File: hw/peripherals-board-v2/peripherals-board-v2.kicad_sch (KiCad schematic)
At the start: 8 parts, among them J1 Screw_Terminal_01x04, J2 Conn_01x04_Socket, U2 M24C01-FMN, U4 AMS1117-5.0

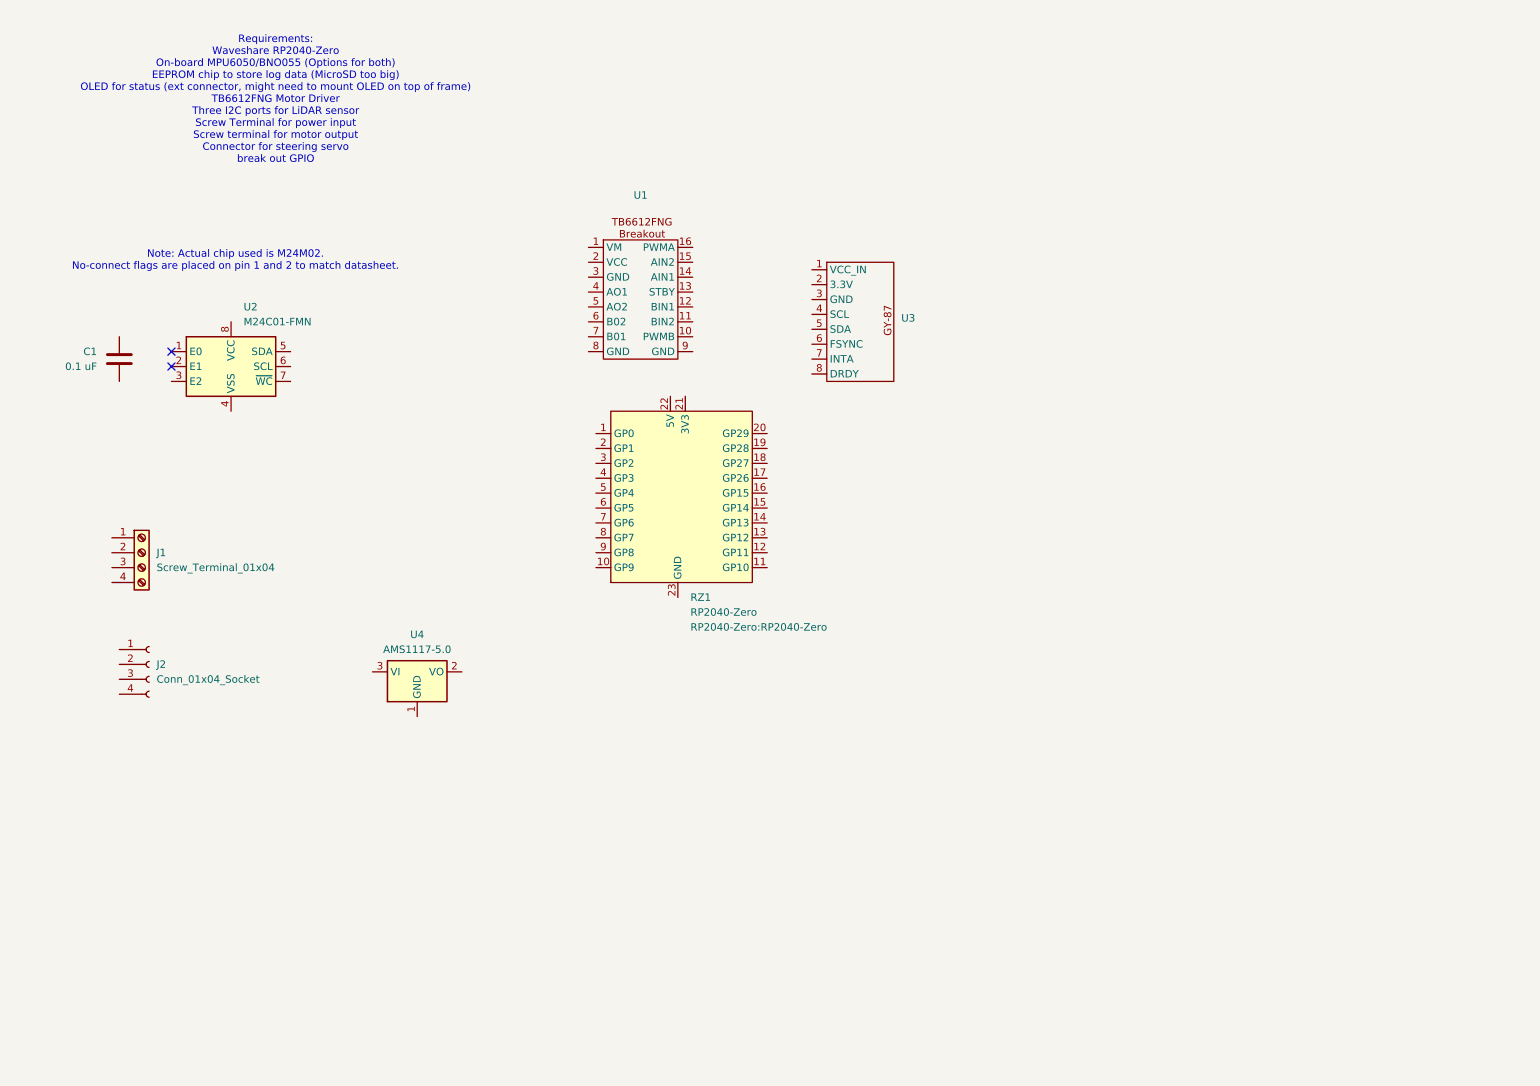
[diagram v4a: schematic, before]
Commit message: Revision 1 of PCB layout, create footprints, generate interactive BOM
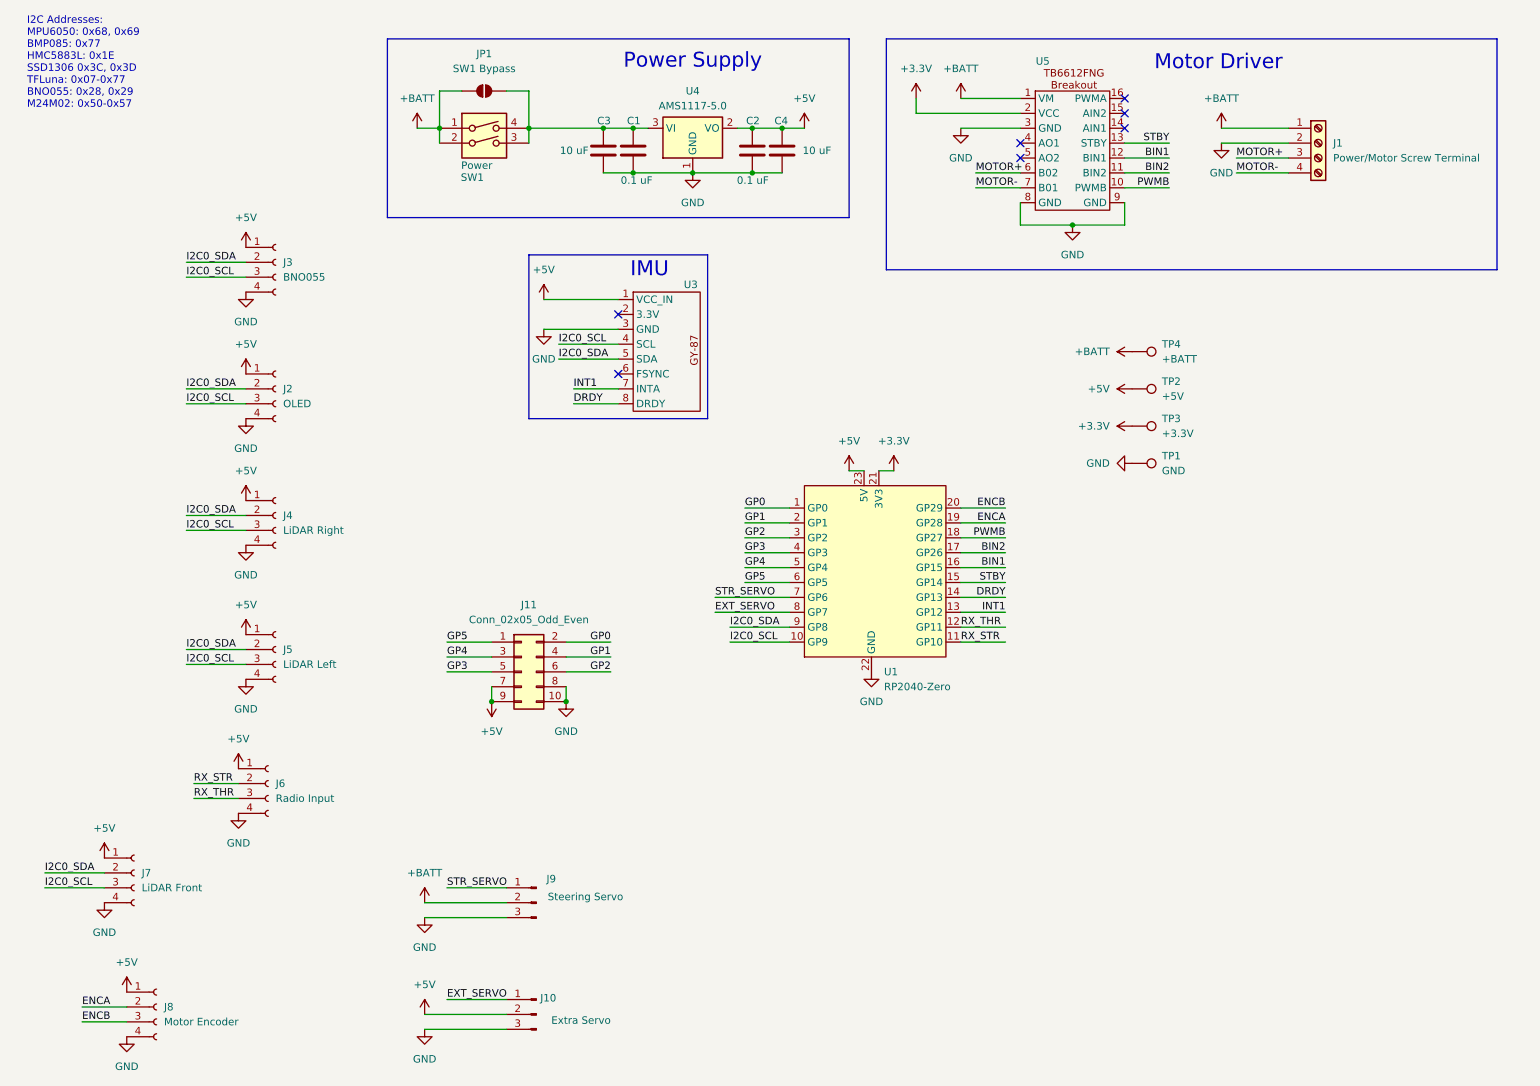
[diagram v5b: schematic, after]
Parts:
- removed U2: M24C01-FMN, Package_SO:SOIC-8_3.9x4.9mm_P1.27mm, symbol Memory_EEPROM:M24C01-FMN
- added C2: 0.1 uF, Capacitor_SMD:C_0805_2012Metric_Pad1.18x1.45mm_HandSolder, symbol Device:C
- added C3, C4: 10 uF, Capacitor_SMD:C_0805_2012Metric_Pad1.18x1.45mm_HandSolder, symbol Device:C
- added J10: Extra Servo, Connector_PinHeader_2.54mm:PinHeader_1x03_P2.54mm_Vertical, symbol Connector:Conn_01x03_Pin
- added J11: Conn_02x05_Odd_Even, Connector_PinSocket_2.54mm:PinSocket_2x05_P2.54mm_Vertical, symbol Connector_Generic:Conn_02x05_Odd_Even
- added J3: BNO055, Connector_JST:JST_EH_S4B-EH_1x04_P2.50mm_Horizontal, symbol Connector:Conn_01x04_Socket
- added J4: LiDAR Right, Connector_JST:JST_EH_S4B-EH_1x04_P2.50mm_Horizontal, symbol Connector:Conn_01x04_Socket
- added J5: LiDAR Left, Connector_JST:JST_EH_S4B-EH_1x04_P2.50mm_Horizontal, symbol Connector:Conn_01x04_Socket
- added J6: Radio Input, Connector_JST:JST_EH_S4B-EH_1x04_P2.50mm_Horizontal, symbol Connector:Conn_01x04_Socket
- added J7: LiDAR Front, Connector_JST:JST_EH_S4B-EH_1x04_P2.50mm_Horizontal, symbol Connector:Conn_01x04_Socket
- added J8: Motor Encoder, Connector_JST:JST_EH_S4B-EH_1x04_P2.50mm_Horizontal, symbol Connector:Conn_01x04_Socket
- added J9: Steering Servo, Connector_PinHeader_2.54mm:PinHeader_1x03_P2.54mm_Vertical, symbol Connector:Conn_01x03_Pin
- added JP1: SW1 Bypass, Jumper:SolderJumper-2_P1.3mm_Open_RoundedPad1.0x1.5mm, symbol Jumper:SolderJumper_2_Open
- added SW1: Power, Package_DIP:DIP-4_W7.62mm, symbol Switch:SW_DIP_x02
- added TP1: GND, TestPoint:TestPoint_Pad_D1.5mm, symbol Connector:TestPoint
- added TP2: +5V, TestPoint:TestPoint_Pad_D1.5mm, symbol Connector:TestPoint
- added TP3: +3.3V, TestPoint:TestPoint_Pad_D1.5mm, symbol Connector:TestPoint
- added TP4: +BATT, TestPoint:TestPoint_Pad_D1.5mm, symbol Connector:TestPoint
- J1: value Screw_Terminal_01x04 -> Power/Motor Screw Terminal
- J2: value Conn_01x04_Socket -> OLED
- U4: footprint Package_TO_SOT_SMD:TO-263-2 -> Package_TO_SOT_SMD:SOT-223-3_TabPin2
- renumbered RZ1 to U1, U1 to U5
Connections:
- net GP0: now reaches U1.1 (GP0)
- net GP0: now also J11.2 (Pin_2)
- net I2C0_SCL: now reaches U1.10 (GP9)
- net I2C0_SCL: now also J2.3 (Pin_3), U3.4 (SCL), J3.3 (Pin_3), J4.3 (Pin_3), J5.3 (Pin_3), J7.3 (Pin_3)
- net RX_STR: now reaches U1.11 (GP10)
- net RX_STR: now also J6.2 (Pin_2)
- net RX_THR: now reaches U1.12 (GP11)
- net RX_THR: now also J6.3 (Pin_3)
- net INT1: now reaches U1.13 (GP12)
- net INT1: now also U3.7 (INTA)
- net DRDY: now reaches U1.14 (GP13)
- net DRDY: now also U3.8 (DRDY)
- net STBY: now reaches U1.15 (GP14)
- net STBY: now also U5.13 (STBY)
- net BIN1: now reaches U1.16 (GP15)
- net BIN1: now also U5.12 (BIN1)
- net BIN2: now reaches U1.17 (GP26)
- net BIN2: now also U5.11 (BIN2)
- net PWMB: now reaches U1.18 (GP27)
- net PWMB: now also U5.10 (PWMB)
- net ENCA: now reaches U1.19 (GP28)
- net ENCA: now also J8.2 (Pin_2)
- net GP1: now reaches U1.2 (GP1)
- net GP1: now also J11.4 (Pin_4)
- net ENCB: now reaches U1.20 (GP29)
- net ENCB: now also J8.3 (Pin_3)
- net +3.3V: now reaches U1.21 (3V3)
- net +3.3V: now also U5.2 (VCC), TP3.1
- net GND: now reaches U1.22 (GND)
- net GND: now also C1.2, J1.2 (Pin_2), J2.4 (Pin_4), U3.3 (GND), U4.1 (GND), U5.3 (GND), U5.8 (GND), U5.9 (GND), C2.2, C3.2, C4.2, J10.3 (Pin_3), J11.10 (Pin_10), J11.8 (Pin_8), J3.4 (Pin_4), J4.4 (Pin_4), J5.4 (Pin_4), J6.4 (Pin_4), J7.4 (Pin_4), J8.4 (Pin_4), J9.3 (Pin_3), TP1.1
- net +5V: now reaches U1.23 (5V)
- net +5V: now also J2.1 (Pin_1), U3.1 (VCC_IN), U4.2 (VO), C2.1, C4.1, J10.2 (Pin_2), J11.7 (Pin_7), J11.9 (Pin_9), J3.1 (Pin_1), J4.1 (Pin_1), J5.1 (Pin_1), J6.1 (Pin_1), J7.1 (Pin_1), J8.1 (Pin_1), TP2.1
- net GP2: now reaches U1.3 (GP2)
- net GP2: now also J11.6 (Pin_6)
- net GP3: now reaches U1.4 (GP3)
- net GP3: now also J11.5 (Pin_5)
- net GP4: now reaches U1.5 (GP4)
- net GP4: now also J11.3 (Pin_3)
- net GP5: now reaches U1.6 (GP5)
- net GP5: now also J11.1 (Pin_1)
- net STR_SERVO: now reaches U1.7 (GP6)
- net STR_SERVO: now also J9.1 (Pin_1)
- net EXT_SERVO: now reaches U1.8 (GP7)
- net EXT_SERVO: now also J10.1 (Pin_1)
- net I2C0_SDA: now reaches U1.9 (GP8)
- net I2C0_SDA: now also J2.2 (Pin_2), U3.5 (SDA), J3.2 (Pin_2), J4.2 (Pin_2), J5.2 (Pin_2), J7.2 (Pin_2)
- net +BATT: now reaches J1.1 (Pin_1)
- net +BATT: now also U5.1 (VM), J9.2 (Pin_2), JP1.1 (A), SW1.1, SW1.2, TP4.1
- net MOTOR+: now reaches J1.3 (Pin_3)
- net MOTOR+: now also U5.6 (B02)
- net MOTOR-: now reaches J1.4 (Pin_4)
- net MOTOR-: now also U5.7 (B01)
- net at U4.3 (VI): now also C1.1, C3.1, JP1.2 (B), SW1.3, SW1.4
- no-connect marks 2 -> 7
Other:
- note added: "I2C Addresses: MPU6050: 0x68, 0x69 BMP085: 0x77 HMC5883L: 0x1E SSD1306 0x3C, 0x3D TFLuna: 0x07-0x77 BNO055: 0x28, 0x29 M24M02: 0x50-0x57"
- note added: "IMU"
- note added: "Motor Driver"
- note added: "Power Supply"
- note removed: "Note: Actual chip used is M24M02. No-connect flags are placed on pin 1 and 2 to match datasheet."
- note removed: "Requirements: Waveshare RP2040-Zero On-board MPU6050/BNO055 (Options for both) EEPROM chip to store log data (MicroSD too big) OLED for status (ext connector, might need to mount OLED on top of frame) TB6612FNG Motor Driver Three I2C ports for LiDAR sensor Screw Terminal for power input Screw terminal for motor output Connector for steering servo break out GPIO"
- moved on the sheet: C1, J1, J2, U1, U3, U5

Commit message: Reroute PCB
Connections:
- net DRDY: now also U1.13 (GP12); no longer U1.14 (GP13)
- net INT1: now also U1.14 (GP13); no longer U1.13 (GP12)
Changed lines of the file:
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@@
-		)
-	)
-	(label "INT1"
-		(at 180.34 115.57 180)
-		(effects
-			(font
-				(size 1.27 1.27)
-			)
-			(justify right bottom)
 		)
 	)
@@
 		)
 	)
+	(label "DRDY"
+		(at 180.34 115.57 180)
+		(effects
+			(font
+				(size 1.27 1.27)
+			)
+			(justify right bottom)
+		)
+	)
 	(label "BIN2"
 		(at 180.34 105.41 180)
@@
 		)
 	)
-	(label "DRDY"
-		(at 180.34 113.03 180)
-		(effects
-			(font
-				(size 1.27 1.27)
-			)
-			(justify right bottom)
-		)
-	)
 	(label "GP4"
 		(at 85.09 123.19 0)
@@
 		)
 	)
+	(label "INT1"
+		(at 180.34 113.03 180)
+		(effects
+			(font
+				(size 1.27 1.27)
+			)
+			(justify right bottom)
+		)
+	)

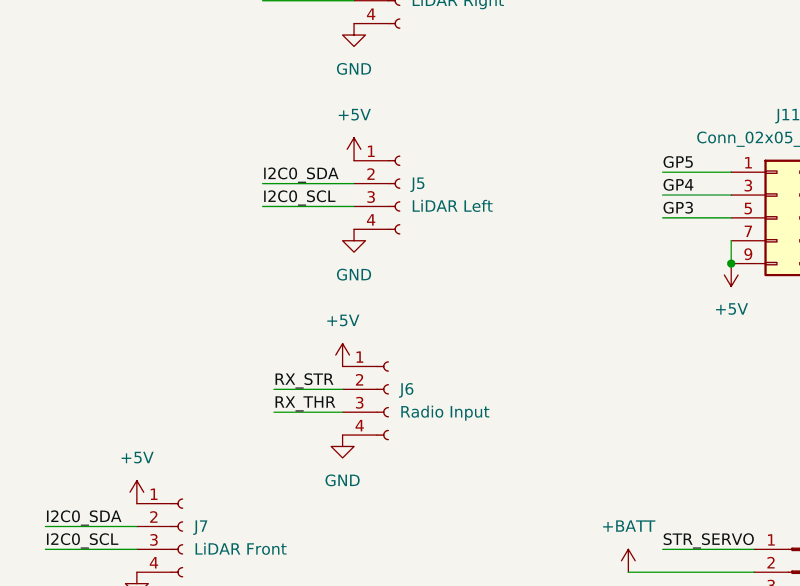
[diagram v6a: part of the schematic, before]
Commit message: Swap left LiDAR and radio input connectors
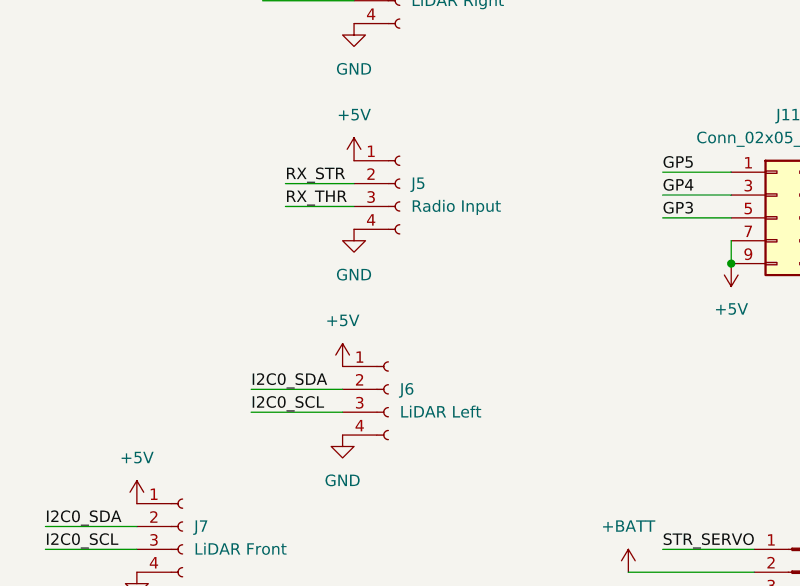
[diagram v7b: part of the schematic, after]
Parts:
- J5: value LiDAR Left -> Radio Input
- J6: value Radio Input -> LiDAR Left
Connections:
- net I2C0_SCL: now also J6.3 (Pin_3); no longer J5.3 (Pin_3)
- net I2C0_SDA: now also J6.2 (Pin_2); no longer J5.2 (Pin_2)
- net RX_STR: now also J5.2 (Pin_2); no longer J6.2 (Pin_2)
- net RX_THR: now also J5.3 (Pin_3); no longer J6.3 (Pin_3)
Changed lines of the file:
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@@
 	(wire
 		(pts
+			(xy 39.37 144.78) (xy 49.53 144.78)
+		)
+		(stroke
+			(width 0)
+			(type default)
+		)
+	)
+	(wire
+		(pts
 			(xy 83.82 33.02) (xy 83.82 35.56)
 		)
@@
 	(wire
 		(pts
-			(xy 40.64 124.46) (xy 50.8 124.46)
+			(xy 43.18 121.92) (xy 50.8 121.92)
 		)
 		(stroke
@@
 	(wire
 		(pts
-			(xy 40.64 121.92) (xy 50.8 121.92)
-		)
-		(stroke
-			(width 0)
-			(type default)
-		)
-	)
-	(wire
-		(pts
 			(xy 158.75 91.44) (xy 161.29 91.44)
 		)
@@
 	(wire
 		(pts
-			(xy 41.91 144.78) (xy 49.53 144.78)
+			(xy 130.81 115.57) (xy 143.51 115.57)
 		)
 		(stroke
@@
 	(wire
 		(pts
-			(xy 130.81 115.57) (xy 143.51 115.57)
+			(xy 40.64 58.42) (xy 50.8 58.42)
 		)
 		(stroke
@@
 	(wire
 		(pts
-			(xy 40.64 58.42) (xy 50.8 58.42)
+			(xy 81.28 184.15) (xy 95.25 184.15)
 		)
 		(stroke
@@
 	(wire
 		(pts
-			(xy 81.28 184.15) (xy 95.25 184.15)
+			(xy 105.41 123.19) (xy 113.03 123.19)
 		)
 		(stroke
@@
 	(wire
 		(pts
-			(xy 105.41 123.19) (xy 113.03 123.19)
+			(xy 165.1 30.48) (xy 182.88 30.48)
 		)
 		(stroke
@@
 	(wire
 		(pts
-			(xy 165.1 30.48) (xy 182.88 30.48)
+			(xy 134.62 33.02) (xy 137.16 33.02)
 		)
 		(stroke
@@
 	(wire
 		(pts
-			(xy 134.62 33.02) (xy 137.16 33.02)
+			(xy 219.71 38.1) (xy 228.6 38.1)
 		)
 		(stroke
@@
 	(wire
 		(pts
-			(xy 219.71 38.1) (xy 228.6 38.1)
+			(xy 39.37 147.32) (xy 49.53 147.32)
 		)
 		(stroke
@@
 	(wire
 		(pts
-			(xy 172.72 113.03) (xy 180.34 113.03)
+			(xy 43.18 124.46) (xy 50.8 124.46)
 		)
 		(stroke
@@
 	(wire
 		(pts
-			(xy 175.26 40.64) (xy 182.88 40.64)
+			(xy 172.72 113.03) (xy 180.34 113.03)
 		)
 		(stroke
@@
 	(wire
 		(pts
-			(xy 41.91 147.32) (xy 49.53 147.32)
+			(xy 175.26 40.64) (xy 182.88 40.64)
 		)
 		(stroke
@@
 		)
 	)
-	(label "RX_STR"
-		(at 41.91 144.78 0)
-		(effects
-			(font
-				(size 1.27 1.27)
-			)
-			(justify left bottom)
-		)
-	)
-	(label "I2C0_SDA"
-		(at 40.64 121.92 0)
-		(effects
-			(font
-				(size 1.27 1.27)
-			)
-			(justify left bottom)
-		)
-	)
 	(label "I2C0_SCL"
 		(at 40.64 80.01 0)
@@
 		)
 	)
-	(label "I2C0_SCL"
-		(at 40.64 124.46 0)
-		(effects
-			(font
-				(size 1.27 1.27)
-			)
-			(justify left bottom)
-		)
-	)
 	(label "I2C0_SDA"
 		(at 40.64 55.88 0)
@@
 		)
 	)
+	(label "RX_THR"
+		(at 43.18 124.46 0)
+		(effects
+			(font
+				(size 1.27 1.27)
+			)
+			(justify left bottom)
+		)
+	)
 	(label "DRDY"
 		(at 106.68 80.01 0)
@@
 		)
 	)
-	(label "RX_THR"
-		(at 41.91 147.32 0)
-		(effects
-			(font
-				(size 1.27 1.27)
-			)
-			(justify left bottom)
-		)
-	)
 	(label "MOTOR-"
 		(at 175.26 43.18 0)
@@
 		)
 	)
+	(label "I2C0_SDA"
+		(at 39.37 144.78 0)
+		(effects
+			(font
+				(size 1.27 1.27)
+			)
+			(justify left bottom)
+		)
+	)
 	(label "ENCA"
 		(at 180.34 100.33 180)
@@
 		)
 	)
+	(label "I2C0_SCL"
+		(at 39.37 147.32 0)
+		(effects
+			(font
+				(size 1.27 1.27)
+			)
+			(justify left bottom)
+		)
+	)
 	(label "STBY"
 		(at 180.34 110.49 180)
@@
 		)
 	)
+	(label "RX_STR"
+		(at 43.18 121.92 0)
+		(effects
+			(font
+				(size 1.27 1.27)
+			)
+			(justify left bottom)
+		)
+	)
 	(symbol
 		(lib_id "power:GND")
@@
 			)
 		)
-		(property "Value" "Radio Input"
+		(property "Value" "LiDAR Left"
 			(at 55.88 147.3199 0)
 			(effects
@@
 			)
 		)
-		(property "Value" "LiDAR Left"
+		(property "Value" "Radio Input"
 			(at 57.15 124.4599 0)
 			(effects
